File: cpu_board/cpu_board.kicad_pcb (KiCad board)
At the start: 2 copper layers, 78.5 x 76.7 mm, 215 parts, among them J1 USB_C_pycubed, J2 JTAG_SWD_10, J3 353620650, J4 353620650, J5 353620650, J6 Conn_01x06, J7 Conn_01x06, J8 DF40C-100DP-0.4V(51), J9 DF40C-100DP-0.4V(51), Q1 IRLML2803, Q2 NDS8434, SW1 SW_DIP_x10, SW2 SW_DIP_x04, U1 TPS7A4501DCQT, U2 MIMXRT1176, U4 EM064LXQADG13IS1T, U5 MT29F1G01ABBFDWB, U6 USBLC6-2SC6, U7 MT48H32M16LFB4-6, U8 TPS54226PWPRPWP14_2P31X2P46-L, U9 TPS54226PWPRPWP14_2P31X2P46-L, Y1 24.0mHz, Y2 32.768kHz, Y3 24.0mHz

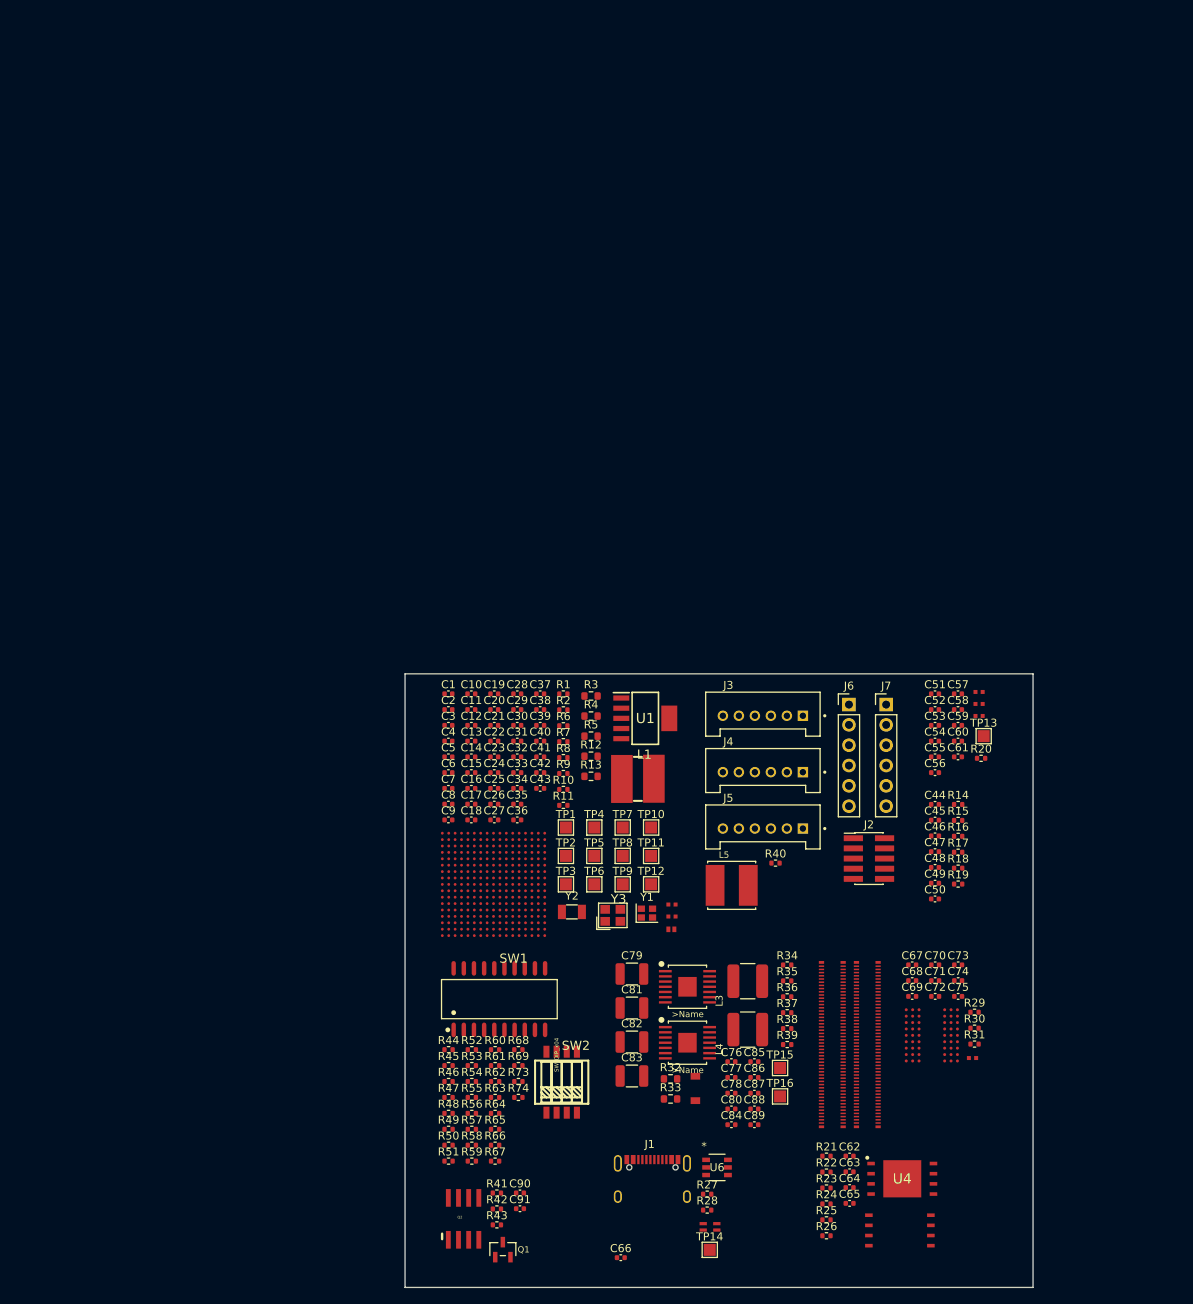
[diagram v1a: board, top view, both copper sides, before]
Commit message: route most of power distribution
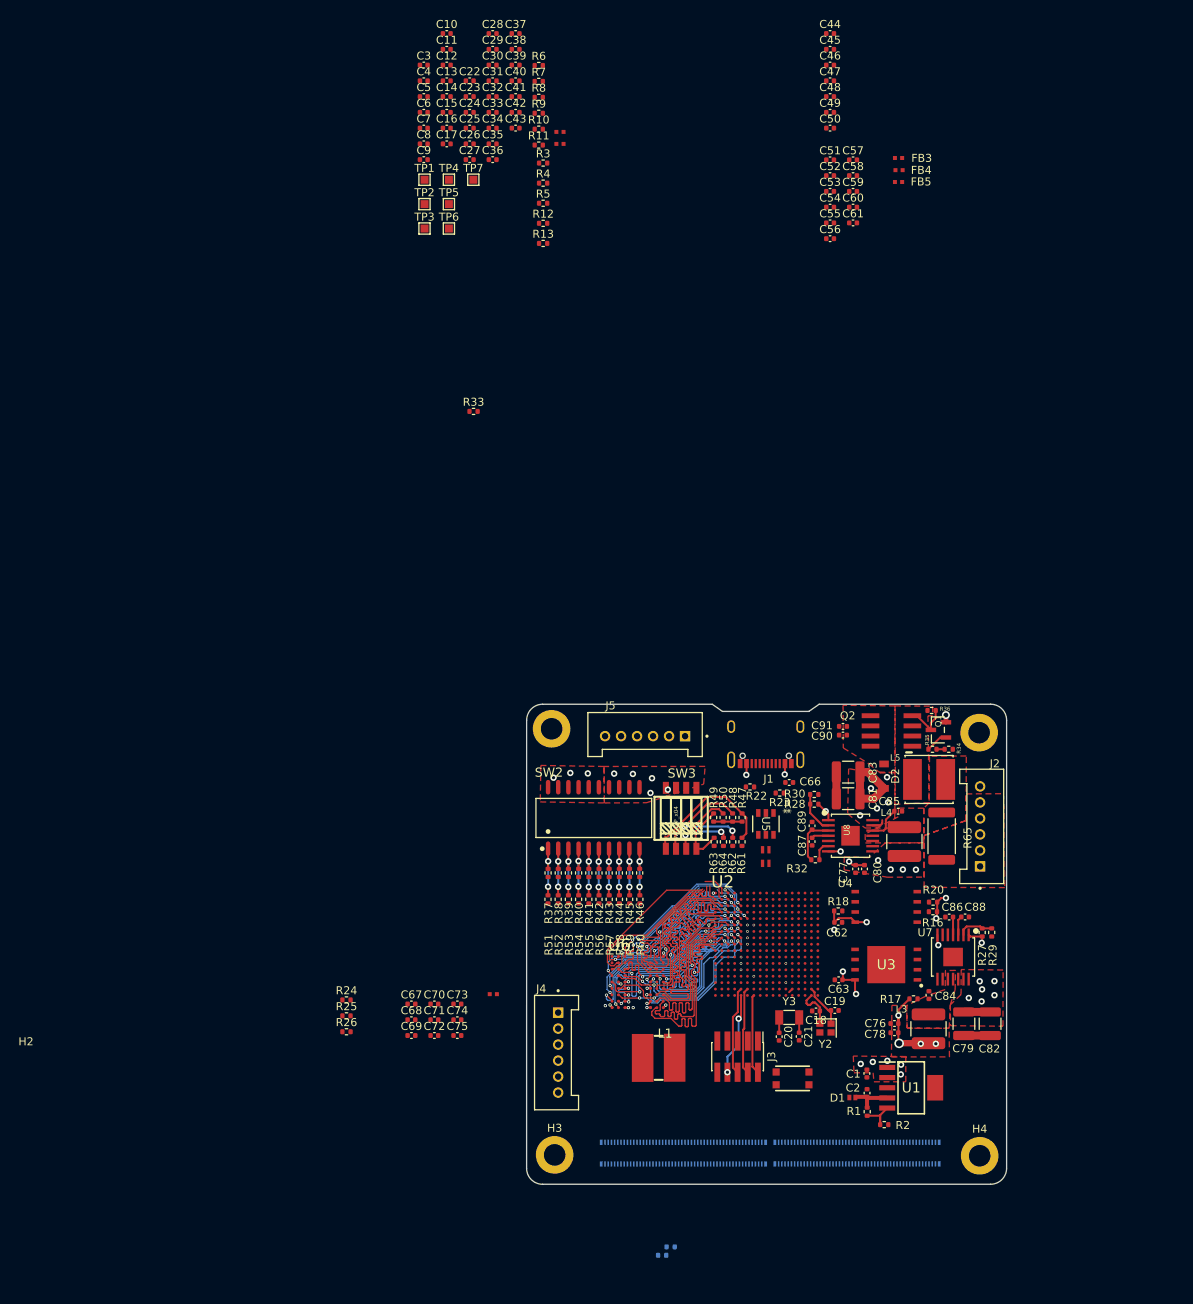
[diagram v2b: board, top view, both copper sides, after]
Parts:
- removed C64, C65: 1uF, Capacitor_SMD:C_0402_1005Metric
- removed J8, J9: DF40C-100DP-0.4V(51), adcs:HIROSE_DF40C-100DP-0.4V(51)
- removed R19: 0Ω, Resistor_SMD:R_0402_1005Metric
- removed R21: 10kΩ, Resistor_SMD:R_0402_1005Metric
- removed R66, R67, R68, R69: 47kΩ, Resistor_SMD:R_0402_1005Metric
- removed R73, R74: 100kΩ, Resistor_SMD:R_0402_1005Metric
- removed TP10, TP11, TP12, TP13, TP14, TP15, TP16, TP8, TP9: TestPoint, TestPoint:TestPoint_Pad_1.5x1.5mm
- removed U9: TPS54226PWPRPWP14_2P31X2P46-L, mainboard:PWP14_2P31X2P46-L
- removed Y1: 24.0mHz, Crystal:Crystal_SMD_2016-4Pin_2.0x1.6mm
- added H1: MountingHole_Pad, MountingHole:MountingHole_2.7mm_M2.5_DIN965_Pad, F.Cu at (74.1, 8.85)
- added H2: MountingHole_Pad, MountingHole:MountingHole_2.7mm_M2.5_DIN965_Pad, F.Cu at (20.6, 8.37)
- added H3: MountingHole_Pad, MountingHole:MountingHole_2.7mm_M2.5_DIN965_Pad, F.Cu at (21.0, 61.6)
- added H4: MountingHole_Pad, MountingHole:MountingHole_2.7mm_M2.5_DIN965_Pad, F.Cu at (74.1, 61.7)
- added SW3: SW_DIP_x04, adcs:SW-SMD_8P-L6.7-W5.4-P1.27-LS8.5, F.Cu at (36.8, 19.6)
- added U3: EM064LXQADG13IS1T, adcs:SON127P800X600X95-9N-D, F.Cu at (62.5, 37.9)
- C18, C19: value 10pF -> 8pF
- C44: value 2.2uF -> 4.7uF
- C45: value 4.7uF -> 2.2uF
- J2: value JTAG_SWD_10 -> 353620650; footprint Connector_PinHeader_1.27mm:PinHeader_2x05_P1.27mm_Vertical_SMD -> mainboard:MOLEX_35362-0650
- J3: value 353620650 -> JTAG_SWD_10; footprint mainboard:MOLEX_35362-0650 -> Connector_PinHeader_1.27mm:PinHeader_2x05_P1.27mm_Vertical_SMD
- J6, J7: value Conn_01x06 -> DF40C-100DP-0.4V(51); footprint Connector_PinHeader_2.54mm:PinHeader_1x06_P2.54mm_Vertical -> adcs:HIROSE_DF40C-100DP-0.4V(51); moved to B.Cu
- R10: value 10kΩ -> 4.7kΩ
- R11: value 100kΩ -> 0Ω
- R12, R13: value 10mΩ -> 0Ω; footprint Resistor_SMD:R_0603_1608Metric -> Resistor_SMD:R_0402_1005Metric
- R14: value DNP -> 0Ω; moved to B.Cu
- R15: value 4.7kΩ -> 0Ω; moved to B.Cu
- R16, R17: value 0Ω -> 10kΩ
- R18, R20: value 0Ω -> 33k
- R22: value 10kΩ -> 5.1kΩ
- R23: value 33k -> 5.1kΩ
- R24: value 33k -> 100kΩ
- R25: value 33k -> 4.7K - DNP
- R26: value 33k -> 0Ω
- R27: value 5.1kΩ -> 30.1kΩ
- R28: value 5.1kΩ -> 73.2kΩ
- R29: value 100kΩ -> 22.1kΩ
- R3: value 1Ω -> 30kΩ; footprint Resistor_SMD:R_0603_1608Metric -> Resistor_SMD:R_0402_1005Metric
- R30: value 4.7K - DNP -> 22.1kΩ
- R31: value 0Ω -> 100kΩ; moved to B.Cu
- R32: value 10mΩ -> 100kΩ; footprint Resistor_SMD:R_0603_1608Metric -> Resistor_SMD:R_0402_1005Metric
- R33: value 10mΩ -> 10kΩ; footprint Resistor_SMD:R_0603_1608Metric -> Resistor_SMD:R_0402_1005Metric
- R34: value 30.1kΩ -> 10kΩ
- R35: value 73.2kΩ -> 4.7kΩ
- R36: value 22.1kΩ -> 100kΩ
- R37: value 22.1kΩ -> 47kΩ
- R38, R39, R43: value 100kΩ -> 47kΩ
- R4: value 10mΩ -> DNP; footprint Resistor_SMD:R_0603_1608Metric -> Resistor_SMD:R_0402_1005Metric
- R40, R41: value 10kΩ -> 47kΩ
- R42: value 4.7kΩ -> 47kΩ
- R44, R45, R46, R47, R48: value 22kΩ -> 47kΩ
- R49, R50: value 22kΩ -> 100kΩ
- R5: value 10mΩ -> 4.7kΩ; footprint Resistor_SMD:R_0603_1608Metric -> Resistor_SMD:R_0402_1005Metric
- R56, R57: value 4.7kΩ -> 22kΩ
- R58, R59, R60, R61, R62: value 47kΩ -> 22kΩ
- R6: value 30kΩ -> 0Ω
- R63, R64: value 47kΩ -> 4.7kΩ
- R65: value 47kΩ -> 10mΩ; footprint Resistor_SMD:R_0402_1005Metric -> Resistor_SMD:R_2512_6332Metric
- R7: value DNP -> 10kΩ
- R8: value 4.7kΩ -> 100kΩ
- R9: value 0Ω -> DNP
- SW1: value SW_DIP_x10 -> SWITCH_SMT4.6X2.8; footprint adcs:SW-SMD_DSHP10TS-S -> mainboard:BTN_KMR2_4.6X2.8
- SW2: value SW_DIP_x04 -> SW_DIP_x10; footprint adcs:SW-SMD_8P-L6.7-W5.4-P1.27-LS8.5 -> adcs:SW-SMD_DSHP10TS-S
- TP1, TP2, TP3, TP4, TP5, TP6, TP7: footprint TestPoint:TestPoint_Pad_1.5x1.5mm -> TestPoint:TestPoint_Pad_1.0x1.0mm
- U4: value EM064LXQADG13IS1T -> MT29F1G01ABBFDWB; footprint adcs:SON127P800X600X95-9N-D -> adcs:UDFN800X600X65-8
- U5: value MT29F1G01ABBFDWB -> USBLC6-2SC6; footprint adcs:UDFN800X600X65-8 -> adcs:SOT23-6L_STM
- U6: value USBLC6-2SC6 -> MT48H32M16LFB4-6; footprint adcs:SOT23-6L_STM -> adcs:BGA54C80P6X9_800X800X100
- U7: value MT48H32M16LFB4-6 -> TPS54226PWPRPWP14_2P31X2P46-L; footprint adcs:BGA54C80P6X9_800X800X100 -> mainboard:PWP14_2P31X2P46-L
- Y2: value 32.768kHz -> 24.0mHz; footprint Crystal:Crystal_SMD_3215-2Pin_3.2x1.5mm -> Crystal:Crystal_SMD_2016-4Pin_2.0x1.6mm
- Y3: value 24.0mHz -> 32.768kHz; footprint adcs:OSC-SMD_4P-L2.5-W2.0-BL -> Crystal:Crystal_SMD_3215-2Pin_3.2x1.5mm
- moved FB1 97.6 mm to (21.7, -66.2)
- moved FB2 97.6 mm to (21.7, -64.7)
- moved C46 97.2 mm to (55.4, -74.6)
- moved C47 97.2 mm to (55.4, -72.6)
- moved C48 97.2 mm to (55.4, -70.7)
- moved C49 97.2 mm to (55.4, -68.7)
- moved C50 97.2 mm to (55.4, -66.7)
- moved C44 97.2 mm to (55.4, -78.5)
- moved C45 97.2 mm to (55.4, -76.6)
- moved R33 89.4 mm to (10.9, -31.3)
- moved Q1 84.7 mm to (68.9, 8.51), turned to 90 degrees
- moved TP6 84.0 mm to (7.78, -54.2)
- moved TP3 83.9 mm to (4.73, -54.2)
- moved TP5 83.5 mm to (7.78, -57.2)
- moved TP2 83.4 mm to (4.73, -57.2)
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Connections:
- C11 pad 1: /RT1176 #1/MCU_DCDC_IN -> VDD_3V3
- C27 pad 1: VDD_SOC_IN_SENSE -> VDD_SOC_IN
- C29 pad 1: DCDC_1V8_OUT_SENSE -> DCDC_1V8_OUT
- C3 pad 2: Net-(U2A-VDD_SNVS_IN) -> VDD_SNVS_3V3
- C32 pad 1: VDD_SOC_IN_SENSE -> VDD_SOC_IN
- C33 pad 1: DCDC_1V8_OUT_SENSE -> DCDC_1V8_OUT
- C35 pad 1: VDD_SOC_IN_SENSE -> VDD_SOC_IN
- C36 pad 1: DCDC_1V8_OUT_SENSE -> DCDC_1V8_OUT
- C37 pad 1: VDD_SOC_IN_SENSE -> VDD_SOC_IN
- C39 pad 1: DCDC_1V8_OUT_SENSE -> DCDC_1V8_OUT
- C5 pad 1: /RT1176 #1/MCU_DCDC_IN -> VDD_3V3
- C51 pad 1: VDD_3V3 -> VDD_1V8
- C53 pad 1: VDD_3V3 -> VDD_1V8
- C55 pad 1: Net-(U2J-GPIO_EMC_B1_39) -> GPIO_EMC_B1_40
- C7 pad 1: /RT1176 #1/MCU_DCDC_IN -> VDD_3V3
- C76 pad 2: VDD_1V8_SENSE -> VDD_1V8
- C77 pad 2: VDD_3V3_SENSE -> VDD_3V3
- C78 pad 2: VDD_1V8_SENSE -> VDD_1V8
- C80 pad 2: VDD_3V3_SENSE -> VDD_3V3
- C84 pad 1: Net-(U8-SW1) -> Net-(U7-SW1)
- C84 pad 2: Net-(U8-VBST) -> Net-(U7-VBST)
- C85 pad 1: Net-(U9-SW1) -> Net-(U8-SW1)
- C85 pad 2: Net-(U9-VBST) -> Net-(U8-VBST)
- C86 pad 1: Net-(U8-SS) -> Net-(U7-SS)
- C87 pad 1: Net-(U9-SS) -> Net-(U8-SS)
- C88 pad 1: Net-(U8-VREG5) -> Net-(U7-VREG5)
- C89 pad 1: Net-(U9-VREG5) -> Net-(U8-VREG5)
- C9 pad 1: VDD_LPSR_IN -> VDD_3V3
- C90 pad 1: /Interface/VBATT -> VBATT
- C90 pad 2: Net-(C90-Pad2) -> GND
- C91 pad 1: /Interface/VBATT -> VBATT
- C91 pad 2: Net-(C90-Pad2) -> GND
- J2 pad 1: VDD_3V3 -> VBATT_IN
- J2 pad 2: SWD_DIO -> GND
- J2 pad 3: GND -> VBATT_IN
- J2 pad 4: SWD_CLK -> GND
- J2 pad 5: GND -> VBATT_IN
- J2 pad 6: JTAG_TDO -> GND
- J3 pad 1: /Interface/POR_B -> VDD_3V3
- J3 pad 2: /Interface/EN_RT1176 -> SWD_DIO
- J3 pad 3: unconnected-(J3-Pad3) -> GND
- J3 pad 4: unconnected-(J3-Pad4) -> SWD_CLK
- J3 pad 5: /Interface/RT1176_TX_TO_HOST -> GND
- J3 pad 6: /Interface/RT1176_RX_FROM_HOST -> JTAG_TDO
- J4 pad 1: Net-(J7-Pin_1) -> /Interface/POR_B
- J4 pad 3: GND -> unconnected-(J4-Pad3)
- J4 pad 4: GNDREF -> unconnected-(J4-Pad4)
- J4 pad 5: /Interface/VBATT_IN -> /Interface/RT1176_TX_TO_HOST
- J4 pad 6: /Interface/VUSB -> /Interface/RT1176_RX_FROM_HOST
- J5 pad 1: /Interface/VBATT_IN -> Net-(J5-Pad1)
- J5 pad 2: GND -> /Interface/EN_RT1176
- J5 pad 3: /Interface/VBATT_IN -> GND
- J5 pad 4: GND -> GNDREF
- J5 pad 5: /Interface/VBATT_IN -> VBATT_IN
- J5 pad 6: GND -> /Interface/VUSB
- J6 pad 1: /Interface/POR_B -> GPIO_LPSR_00
- J6 pad 2: /Interface/EN_RT1176 -> VDD_3V3
- J6 pad 3: unconnected-(J3-Pad3) -> GPIO_LPSR_01
- J6 pad 4: unconnected-(J3-Pad4) -> VDD_3V3
- J6 pad 5: /Interface/RT1176_TX_TO_HOST -> GPIO_LPSR_02
- J6 pad 6: /Interface/RT1176_RX_FROM_HOST -> VDD_3V3
- J7 pad 1: Net-(J7-Pin_1) -> VDD_3V3_SENSE
- J7 pad 2: /Interface/EN_RT1176 -> MCM_3V3_SENSE
- J7 pad 3: GND -> VDD_3V3
- J7 pad 4: GNDREF -> MCM_3V3
- J7 pad 5: /Interface/VBATT_IN -> VDD_3V3
- J7 pad 6: /Interface/VUSB -> GND
- L2 pad 1: Net-(U6-IO_1_OUT) -> Net-(U5-IO_2_OUT)
- L2 pad 4: Net-(U6-IO_2_OUT) -> Net-(U5-IO_1_OUT)
- L3 pad 1: Net-(U8-SW1) -> Net-(U7-SW1)
- L3 pad 2: VDD_1V8_SENSE -> VDD_1V8
- L4 pad 1: Net-(U9-SW1) -> Net-(U8-SW1)
- L4 pad 2: VDD_3V3_SENSE -> VDD_3V3
- L5 pad 1: /Interface/VBATT_IN -> Net-(L5-Pad1)
- L5 pad 2: /Interface/Power Enable/VBUS_IN -> /Interface/VSYS_IN
- Q2 pad 1: /Interface/Power Enable/VBUS_IN -> /Interface/VSYS_IN
- Q2 pad 2: /Interface/Power Enable/VBUS_IN -> /Interface/VSYS_IN
- Q2 pad 3: /Interface/Power Enable/VBUS_IN -> /Interface/VSYS_IN
- Q2 pad 5: /Interface/VBATT -> VBATT
- Q2 pad 6: /Interface/VBATT -> VBATT
- Q2 pad 7: /Interface/VBATT -> VBATT
- Q2 pad 8: /Interface/VBATT -> VBATT
- R10 pad 1: POR_B -> GND
- R10 pad 2: VDD_SNVS_ANA -> JTAG_MOD
- R11 pad 1: PMIC_ON_REQ -> Net-(U2I-NVCC_DISP1)
- R11 pad 2: VDD_SNVS_ANA -> VDD_1V8
- R12 pad 1: VDD_SOC_IN_SENSE -> Net-(U2I-NVCC_DISP2)
- R12 pad 2: VDD_SOC_IN -> VDD_3V3
- R13 pad 1: DCDC_1V8_OUT_SENSE -> Net-(U2G-NVCC_SD1)
- R13 pad 2: DCDC_1V8_OUT -> VDD_1V8
- R14 pad 1: JTAG_MOD -> Net-(U2G-NVCC_SD2)
- R15 pad 1: GND -> Net-(U2K-VDD_MIPI_1P0)
- R15 pad 2: JTAG_MOD -> VDDA_1P0
- R16 pad 1: Net-(U2I-NVCC_DISP1) -> VDD_1V8
- R16 pad 2: VDD_1V8 -> FlexSPI_A_SS0
- R17 pad 1: Net-(U2I-NVCC_DISP2) -> VDD_1V8
- R17 pad 2: VDD_3V3 -> FlexSPI_A_SS1
- R18 pad 1: Net-(U2G-NVCC_SD1) -> VDD_1V8
- R18 pad 2: VDD_1V8 -> FlexSPI_A_D3
- R20 pad 1: Net-(U2K-VDD_MIPI_1P0) -> VDD_1V8
- R20 pad 2: VDDA_1P0 -> FlexSPI_A_D2
- R22 pad 1: VDD_1V8 -> GNDREF
- R22 pad 2: FlexSPI_A_SS0 -> USB_CC2
- R23 pad 1: VDD_1V8 -> GNDREF
- R23 pad 2: FlexSPI_A_D3 -> USB_CC1
- R24 pad 1: VDD_1V8 -> SEMC_CKE
- R24 pad 2: FlexSPI_A_D3 -> GND
- R25 pad 1: VDD_1V8 -> /SDRAM/SDRAM_1V8
- R25 pad 2: FlexSPI_A_D2 -> SEMC_CS0
- R26 pad 1: VDD_1V8 -> SEMC_CLK
- R26 pad 2: FlexSPI_A_D2 -> /SDRAM/SEMC_CLK_R
- R27 pad 1: GNDREF -> Net-(U7-VFB)
- R27 pad 2: USB_CC2 -> VDD_1V8
- R28 pad 1: GNDREF -> Net-(U8-VFB)
- R28 pad 2: USB_CC1 -> VDD_3V3
- R29 pad 1: SEMC_CKE -> GND
- R29 pad 2: GND -> Net-(U7-VFB)
- R3 pad 1: VDD_SNVS_3V3 -> VDD_3V3
- R3 pad 2: Net-(U2A-VDD_SNVS_IN) -> Net-(U2C-DCDC_PSWITCH)
- R30 pad 1: /SDRAM/SDRAM_1V8 -> GND
- R30 pad 2: SEMC_CS0 -> Net-(U8-VFB)
- R31 pad 1: SEMC_CLK -> Net-(U7-PG)
- R31 pad 2: /SDRAM/SEMC_CLK_R -> Net-(U7-VREG5)
- R32 pad 1: VDD_1V8 -> Net-(U8-PG)
- R32 pad 2: VDD_1V8_SENSE -> Net-(U8-VREG5)
- R33 pad 2: VDD_3V3_SENSE -> Net-(J5-Pad1)
- R34 pad 1: Net-(U8-VFB) -> /Interface/EN_RT1176
- R34 pad 2: VDD_1V8_SENSE -> GND
- R35 pad 1: Net-(U9-VFB) -> /Interface/EN_RT1176
- R35 pad 2: VDD_3V3_SENSE -> Net-(Q1-G)
- R36 pad 1: GND -> /Interface/VSYS_IN
- R36 pad 2: Net-(U8-VFB) -> Net-(Q1-D)
- R37 pad 2: Net-(U9-VFB) -> Net-(R37-Pad2)
- R38 pad 1: Net-(U8-PG) -> GND
- R38 pad 2: Net-(U8-VREG5) -> Net-(R38-Pad2)
- R39 pad 1: Net-(U9-PG) -> GND
- R39 pad 2: Net-(U9-VREG5) -> Net-(R39-Pad2)
- R4 pad 1: VDD_LPSR_IN -> Net-(U2C-DCDC_MODE)
- R4 pad 2: VDD_LPSR_IN -> VDD_3V3
- R40 pad 1: VDD_3V3 -> GND
- R40 pad 2: Net-(J7-Pin_1) -> Net-(R40-Pad2)
- R41 pad 1: /Interface/EN_RT1176 -> GND
- R41 pad 2: GND -> Net-(R41-Pad2)
- R42 pad 1: /Interface/EN_RT1176 -> GND
- R42 pad 2: Net-(Q1-G) -> Net-(R42-Pad2)
- R43 pad 1: /Interface/Power Enable/VBUS_IN -> GND
- R43 pad 2: Net-(Q1-D) -> Net-(R43-Pad2)
- R44 pad 1: Net-(R44-Pad1) -> GND
- R44 pad 2: ENET_RGMII_TXD3 -> Net-(R44-Pad2)
- R45 pad 1: Net-(R45-Pad1) -> GND
- R45 pad 2: ENET_RGMII_TXD2 -> Net-(R45-Pad2)
- R46 pad 1: Net-(R46-Pad1) -> GND
- R46 pad 2: ENET_RGMII_TXD1 -> Net-(R46-Pad2)
- R47 pad 1: Net-(R47-Pad1) -> GND
- R47 pad 2: ENET_RGMII_TXD0 -> Net-(R47-Pad2)
- R48 pad 1: Net-(R48-Pad1) -> GND
- R48 pad 2: ENET_RGMII_TX_EN -> Net-(R48-Pad2)
- R49 pad 1: Net-(R49-Pad1) -> GND
- R49 pad 2: ENET_RGMII_TXC -> Net-(R49-Pad2)
- R5 pad 1: VDD_3V3 -> GND
- R5 pad 2: /RT1176 #1/MCU_DCDC_IN -> Net-(U2C-DCDC_MODE)
- R50 pad 1: Net-(R50-Pad1) -> GND
- R50 pad 2: GPIO_DISP_B2_00 -> Net-(R50-Pad2)
- R51 pad 1: Net-(R51-Pad1) -> Net-(R37-Pad2)
- R51 pad 2: GPIO_DISP_B2_01 -> ENET_RGMII_TXD3_BT
- R52 pad 1: Net-(R52-Pad1) -> Net-(R38-Pad2)
- R52 pad 2: GPIO_DISP_B2_02 -> ENET_RGMII_TXD2_BT
- R53 pad 1: Net-(R53-Pad1) -> Net-(R39-Pad2)
- R53 pad 2: GPIO_DISP_B2_03 -> ENET_RGMII_TXD1_BT
- R54 pad 1: Net-(R54-Pad1) -> Net-(R40-Pad2)
- R54 pad 2: GPIO_DISP_B2_04 -> ENET_RGMII_TXD0_BT
- R55 pad 1: Net-(R55-Pad1) -> Net-(R41-Pad2)
- R55 pad 2: GPIO_DISP_B2_05 -> ENET_RGMII_TX_EN_BT
- R56 pad 1: Net-(R56-Pad1) -> Net-(R42-Pad2)
- R56 pad 2: GPIO_LPSR_02 -> ENET_RGMII_TXC_BT
- R57 pad 1: Net-(R57-Pad1) -> Net-(R43-Pad2)
- R57 pad 2: GPIO_LPSR_03 -> GPIO_DISP_B2_00
- R58 pad 1: GND -> Net-(R44-Pad2)
- R58 pad 2: Net-(R44-Pad1) -> GPIO_DISP_B2_01
- R59 pad 1: GND -> Net-(R45-Pad2)
- R59 pad 2: Net-(R45-Pad1) -> GPIO_DISP_B2_02
- R6 pad 1: /RT1176 #1/MCU_DCDC_IN -> GND
- R6 pad 2: Net-(U2C-DCDC_PSWITCH) -> Net-(U2A-TEST_MODE)
- R60 pad 1: GND -> Net-(R46-Pad2)
- R60 pad 2: Net-(R46-Pad1) -> GPIO_DISP_B2_03
- R61 pad 1: GND -> Net-(R47-Pad2)
- R61 pad 2: Net-(R47-Pad1) -> GPIO_DISP_B2_04
- R62 pad 1: GND -> Net-(R48-Pad2)
- R62 pad 2: Net-(R48-Pad1) -> GPIO_DISP_B2_05
- R63 pad 1: GND -> Net-(R49-Pad2)
- R63 pad 2: Net-(R49-Pad1) -> GPIO_LPSR_02
- R64 pad 1: GND -> Net-(R50-Pad2)
- R64 pad 2: Net-(R50-Pad1) -> GPIO_LPSR_03
- R65 pad 1: GND -> VBATT_IN
- R65 pad 2: Net-(R51-Pad1) -> Net-(L5-Pad1)
- R7 pad 1: Net-(U2C-DCDC_MODE) -> POR_B
- R7 pad 2: /RT1176 #1/MCU_DCDC_IN -> VDD_SNVS_ANA
- R8 pad 1: GND -> PMIC_ON_REQ
- R8 pad 2: Net-(U2C-DCDC_MODE) -> VDD_SNVS_ANA
- R9 pad 1: GND -> JTAG_MOD
- R9 pad 2: Net-(U2A-TEST_MODE) -> VDD_1V8
- SW2 pad 1: Net-(R54-Pad1) -> Net-(R37-Pad2)
- SW2 pad 2: Net-(R55-Pad1) -> Net-(R38-Pad2)
- SW2 pad 3: Net-(R57-Pad1) -> Net-(R39-Pad2)
- SW2 pad 4: Net-(R56-Pad1) -> Net-(R40-Pad2)
- SW2 pad 5: VDD_3V3 -> Net-(R41-Pad2)
- SW2 pad 6: VDD_3V3 -> Net-(R42-Pad2)
- SW2 pad 7: VDD_3V3 -> Net-(R43-Pad2)
- SW2 pad 8: VDD_3V3 -> Net-(R44-Pad2)
- TP1 pad 1: VDD_SNVS_3V3 -> Net-(U2E-CLK1_P)
- TP2 pad 1: VDD_LPSR_IN -> Net-(U2E-CLK1_N)
- TP3 pad 1: VDD_3V3 -> FlexSPI_A_SS1
- TP4 pad 1: Net-(U2A-VDD_SNVS_IN) -> GPIO_EMC_B2_18
- TP5 pad 1: VDD_LPSR_IN -> GPIO_EMC_B1_40
- TP6 pad 1: /RT1176 #1/MCU_DCDC_IN -> GPIO_EMC_B1_41
- TP7 pad 1: Net-(U2E-CLK1_P) -> VUSB
- U2 pad A10: MIPI_DSI_D1_N -> unconnected-(U2K-MIPI_DSI_DN1-PadA10)
- U2 pad A16: WIFI_SDIO_D3 -> GPIO_SD_B1_05
- U2 pad A8: MIPI_DSI_D0_N -> unconnected-(U2K-MIPI_DSI_D0_N-PadA8)
- U2 pad A9: MIPI_DSI_CK_N -> unconnected-(U2K-MIPI_DSI_CKN-PadA9)
- U2 pad B10: MIPI_DSI_D1_P -> unconnected-(U2K-MIPI_DSI_DP1-PadB10)
- U2 pad B15: WIFI_SDIO_D2 -> GPIO_SD_B1_04
- U2 pad B16: WIFI_SDIO_CMD -> GPIO_SD_B1_00
- U2 pad B17: WIFI_SDIO_D1 -> GPIO_SD_B1_03
- U2 pad B8: MIPI_DSI_D0_P -> unconnected-(U2K-MIPI_DSI_D0_P-PadB8)
- U2 pad B9: MIPI_DSI_CK_P -> unconnected-(U2K-MIPI_DSI_CKP-PadB9)
- U2 pad C15: FlexSPI_A_SS0 -> FlexSPI_A_SS1
- U2 pad D15: WIFI_SDIO_CLK -> GPIO_SD_B1_01
- U2 pad E16: OTG_D_N -> OTG1_D_N
- U2 pad E17: OTG_D_P -> OTG1_D_P
- U2 pad F6: VDD_3V3 -> VDD_1V8
- U2 pad F7: VDD_3V3 -> VDD_1V8
- U2 pad G6: VDD_3V3 -> VDD_1V8
- U2 pad J2: Net-(U2J-GPIO_EMC_B1_39) -> GPIO_EMC_B1_40
- U2 pad K1: LPUART6_TXD -> GPIO_EMC_B1_40
- U2 pad K2: LPUART6_CTS -> GPIO_EMC_B2_00
- U2 pad K4: LPUART6_RTS -> GPIO_EMC_B2_01
- U2 pad K5: TPU_BOOT_FAIL -> GPIO_EMC_B2_13
- U2 pad K8: VDD_SOC_IN_SENSE -> VDD_SOC_IN
- U2 pad K9: VDD_SOC_IN_SENSE -> VDD_SOC_IN
- U2 pad L1: LPUART6_RXD -> GPIO_EMC_B1_41
- U2 pad L2: TPU_POW_EN -> GPIO_EMC_B2_15
- U2 pad L5: /RT1176 #1/MCU_DCDC_IN -> VDD_3V3
- U2 pad L8: VDD_SOC_IN_SENSE -> VDD_SOC_IN
- U2 pad L9: BRD_STAT_LED -> GPIO_SNVS_02
- U2 pad M10: USER_LED -> GPIO_SNVS_03
- U2 pad M4: TPU_RST_L -> GPIO_EMC_B2_14
- U2 pad M5: /RT1176 #1/MCU_DCDC_IN -> VDD_3V3
- U2 pad M7: DCDC_1V8_OUT_SENSE -> DCDC_1V8_OUT
- U2 pad M8: DCDC_1V8_OUT_SENSE -> DCDC_1V8_OUT
- U2 pad N3: /RT1176 #3/SEMC_DQS4 -> GPIO_EMC_B2_18
- U2 pad N5: /RT1176 #1/MCU_DCDC_IN -> VDD_3V3
- U2 pad P10: DA_GPIO0 -> GPIO_SNVS_01
- U2 pad P2: MCM_1V8 -> GPIO_EMC_B2_16
- U2 pad P9: CAMERA_INT -> GPIO_SNVS_05
- U2 pad R1: ETHPHY_RST_B -> GPIO_EMC_B2_03
- U2 pad R10: USER_BUTTON -> GPIO_SNVS_00
- U2 pad R11: WIFI_POWER_EN -> GPIO_SNVS_09
- U2 pad R12: VDD_LPSR_IN -> VDD_3V3
- U2 pad R15: USB_PORT_RT -> GPIO_AD_08
- U2 pad R16: USB_OTG1_ID -> GPIO_AD_09
- U2 pad U12: Net-(U2A-VDD_SNVS_IN) -> VDD_SNVS_3V3
- U5 pad 1: FlexSPI_A_SS0 -> /USB-C/USB_DN_CON
- U5 pad 2: FlexSPI_A_D1 -> GND
- U5 pad 3: FlexSPI_A_D2 -> /USB-C/USB_DP_CON
- U5 pad 4: GND -> Net-(U5-IO_2_OUT)
- U5 pad 5: FlexSPI_A_D0 -> VUSB
- U5 pad 6: FlexSPI_A_CLK -> Net-(U5-IO_1_OUT)
- U8 pad 1: VDD_1V8_SENSE -> VDD_3V3
- Y2 pad 1: Net-(U2A-RTC_XTALO) -> Net-(U2E-XTALO)
- Y2 pad 2: Net-(U2A-RTC_XTALI) -> Net-(U2E-XTALI)
- Y3 pad 1: VDD_LPSR_IN -> Net-(U2A-RTC_XTALO)
- Y3 pad 2: GND -> Net-(U2A-RTC_XTALI)
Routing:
- net SEMC_A2: track 0.00 -> 37.0 mm, vias 0 -> 2
- net VDD_1V8: track 0.00 -> 27.2 mm, vias 0 -> 16
- net SEMC_D11: track 0.00 -> 25.0 mm
- net SEMC_D15: track 0.00 -> 24.9 mm
- net SEMC_D13: track 0.00 -> 24.8 mm
- net SEMC_D12: track 0.00 -> 24.7 mm
- net SEMC_D10: track 0.00 -> 24.7 mm
- net SEMC_D14: track 0.00 -> 24.6 mm
- net SEMC_D9: track 0.00 -> 24.6 mm
- net SEMC_DM1: track 0.00 -> 24.5 mm, vias 0 -> 2
- net SEMC_D4: track 0.00 -> 22.6 mm, vias 0 -> 2
- net SEMC_CS0: track 0.00 -> 22.3 mm, vias 0 -> 2
- net SEMC_D3: track 0.00 -> 22.1 mm, vias 0 -> 2
- net SEMC_D6: track 0.00 -> 22.0 mm, vias 0 -> 2
- net SEMC_D5: track 0.00 -> 22.0 mm, vias 0 -> 2
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- added copper zone on F.Cu, net /Interface/VSYS_IN
- added copper zone on In1.Cu, net GND
- added copper zone on In2.Cu, net GND
- added copper zone on In3.Cu, net GND
- added copper zone on In4.Cu, net GND
- added copper zone on F.Cu, net Net-(L5-Pad1)
- added copper zone on F.Cu, net Net-(U7-SW1)
- added copper zone on F.Cu, net Net-(U8-SW1)
- added copper zone on F.Cu, net VBATT
- added copper zone on F.Cu, net VBATT_IN
- added copper zone on F.Cu, net VDD_1V8
- added copper zone on In3.Cu, net VDD_1V8
- added copper zone on F.Cu, net VDD_3V3
- added copper zone on In3.Cu, net VDD_3V3
- added copper zone on F.Cu, net VSYS
- added copper zone on In3.Cu, net VSYS
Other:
- board size 78.5 x 76.7 mm -> 60 x 60 mm
- copper layers 2 -> 6
- board text added: "JLCPCB offers free Via-in-pad for 6-20 layer boards: https://jlcpcb.com/blog/32-Free-Via-in-Pad-on-6-20-Layer-PCBs-with-POFV"

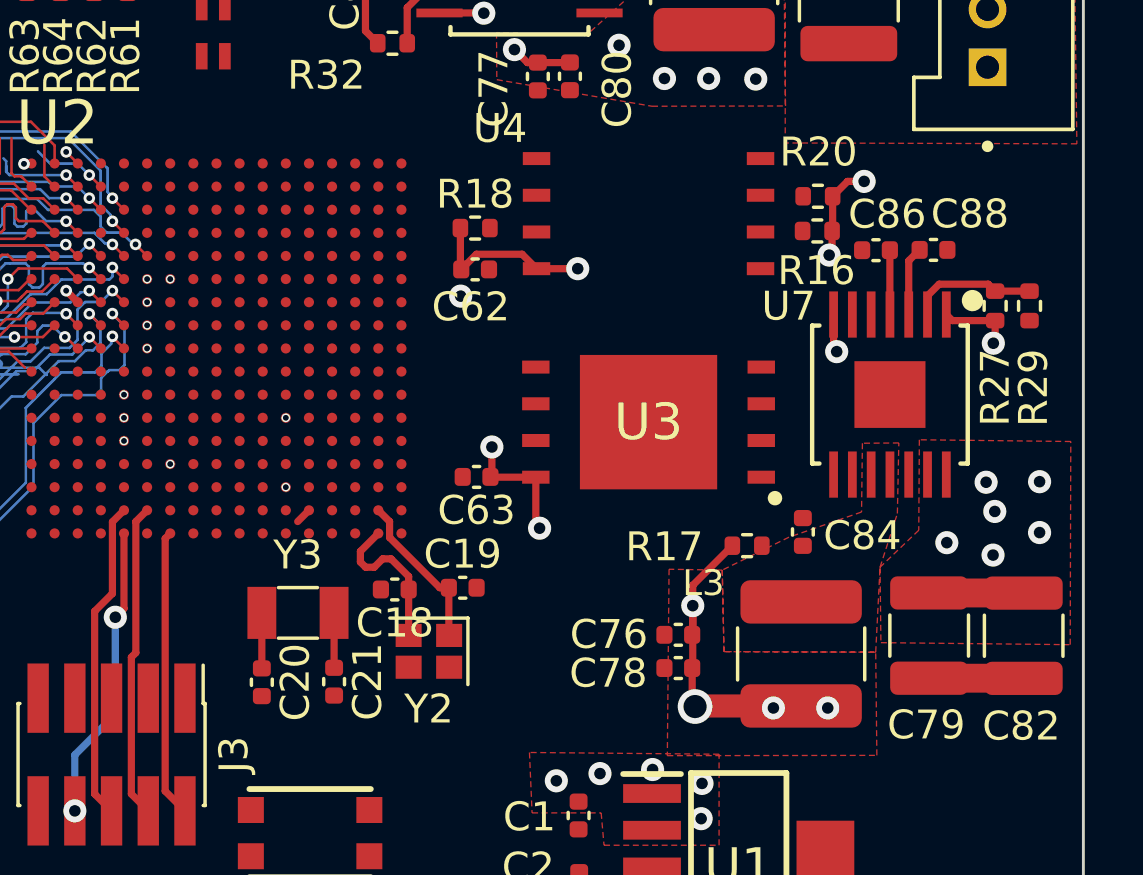
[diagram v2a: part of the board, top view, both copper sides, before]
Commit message: clean up pwr slightly
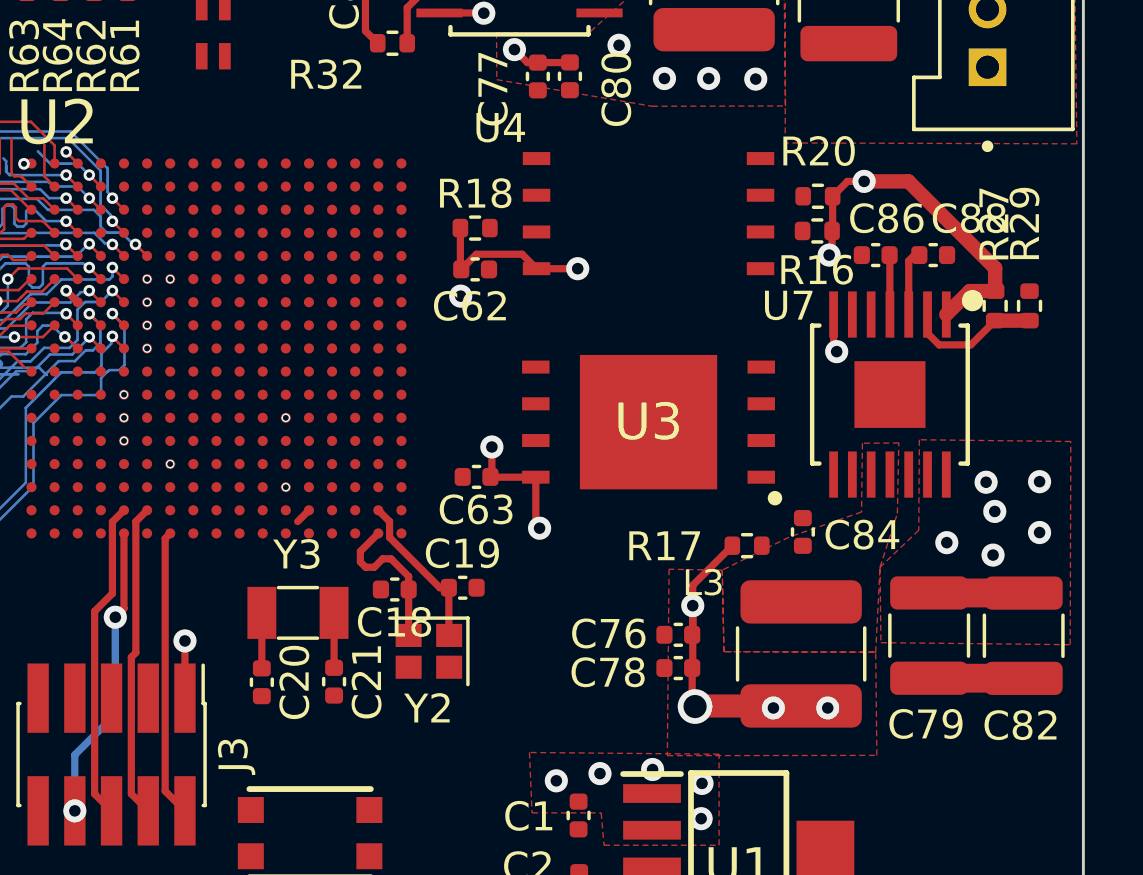
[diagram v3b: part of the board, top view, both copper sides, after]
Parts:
- moved C88 0.18 mm to (72.3, 32.1)
- moved C86 0.17 mm to (70.3, 32.1)
- turned R27 to 90 degrees
- turned R29 to -90 degrees
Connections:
- J7 pad 1: VDD_3V3_SENSE -> VDD_3V3
- J7 pad 10: DCDC_1V8_OUT -> VDD_1V8
- J7 pad 12: GND -> VDD_1V8
- J7 pad 14: VDD_SOC_IN_SENSE -> VDD_1V8
- J7 pad 16: VDD_SOC_IN -> VDD_1V8
- J7 pad 2: MCM_3V3_SENSE -> VDD_3V3
- J7 pad 4: MCM_3V3 -> VDD_3V3
- J7 pad 6: GND -> VDD_3V3
- J7 pad 8: DCDC_1V8_OUT_SENSE -> VDD_3V3
- J7 pad 9: VDD_1V8_SENSE -> VDD_1V8
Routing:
- net VDD_1V8: track 27.2 -> 33.2 mm, vias 16 -> 15
- net VDD_3V3: track 4.64 -> 6.62 mm, vias 19 -> 20
- net Net-(U7-VFB): track 4.44 -> 5.34 mm
